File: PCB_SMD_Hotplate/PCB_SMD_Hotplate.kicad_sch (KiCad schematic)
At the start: 17 parts, among them J1 USB_C_Receptacle_USB2.0_16P, J2 CONN_POWER, U1 ATmega328P-A, U2 CH340C, U3 LM7805_TO220, U4 ICL7660, U5 LM324

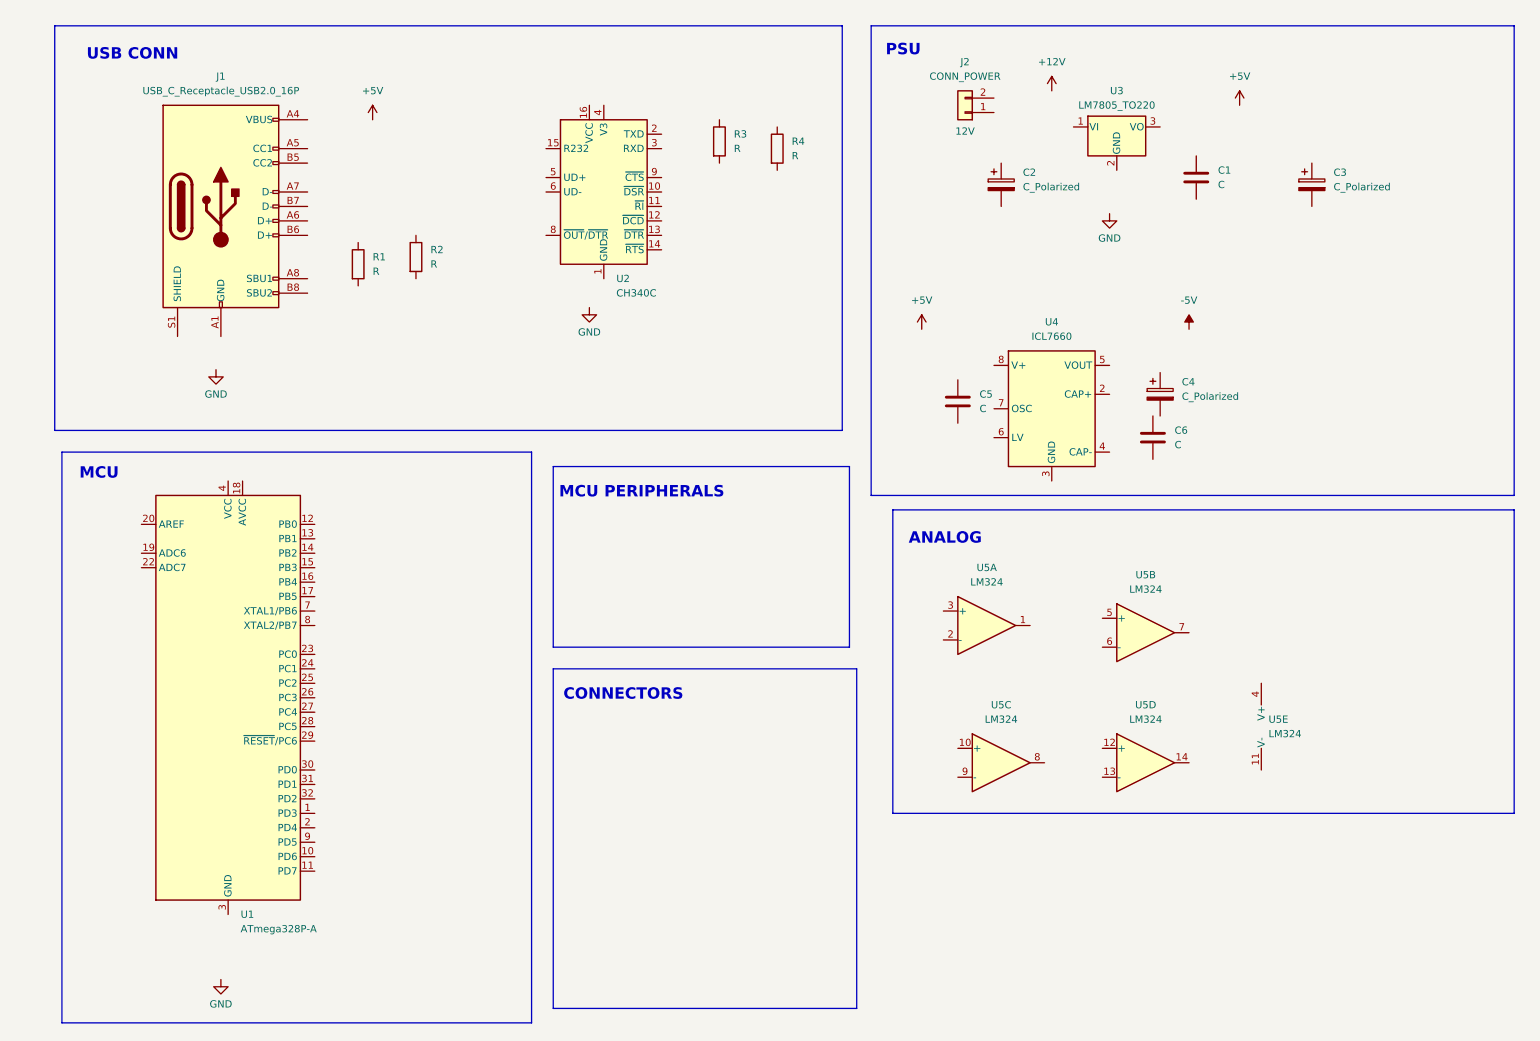
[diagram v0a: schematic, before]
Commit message: Update schematic, start PCB
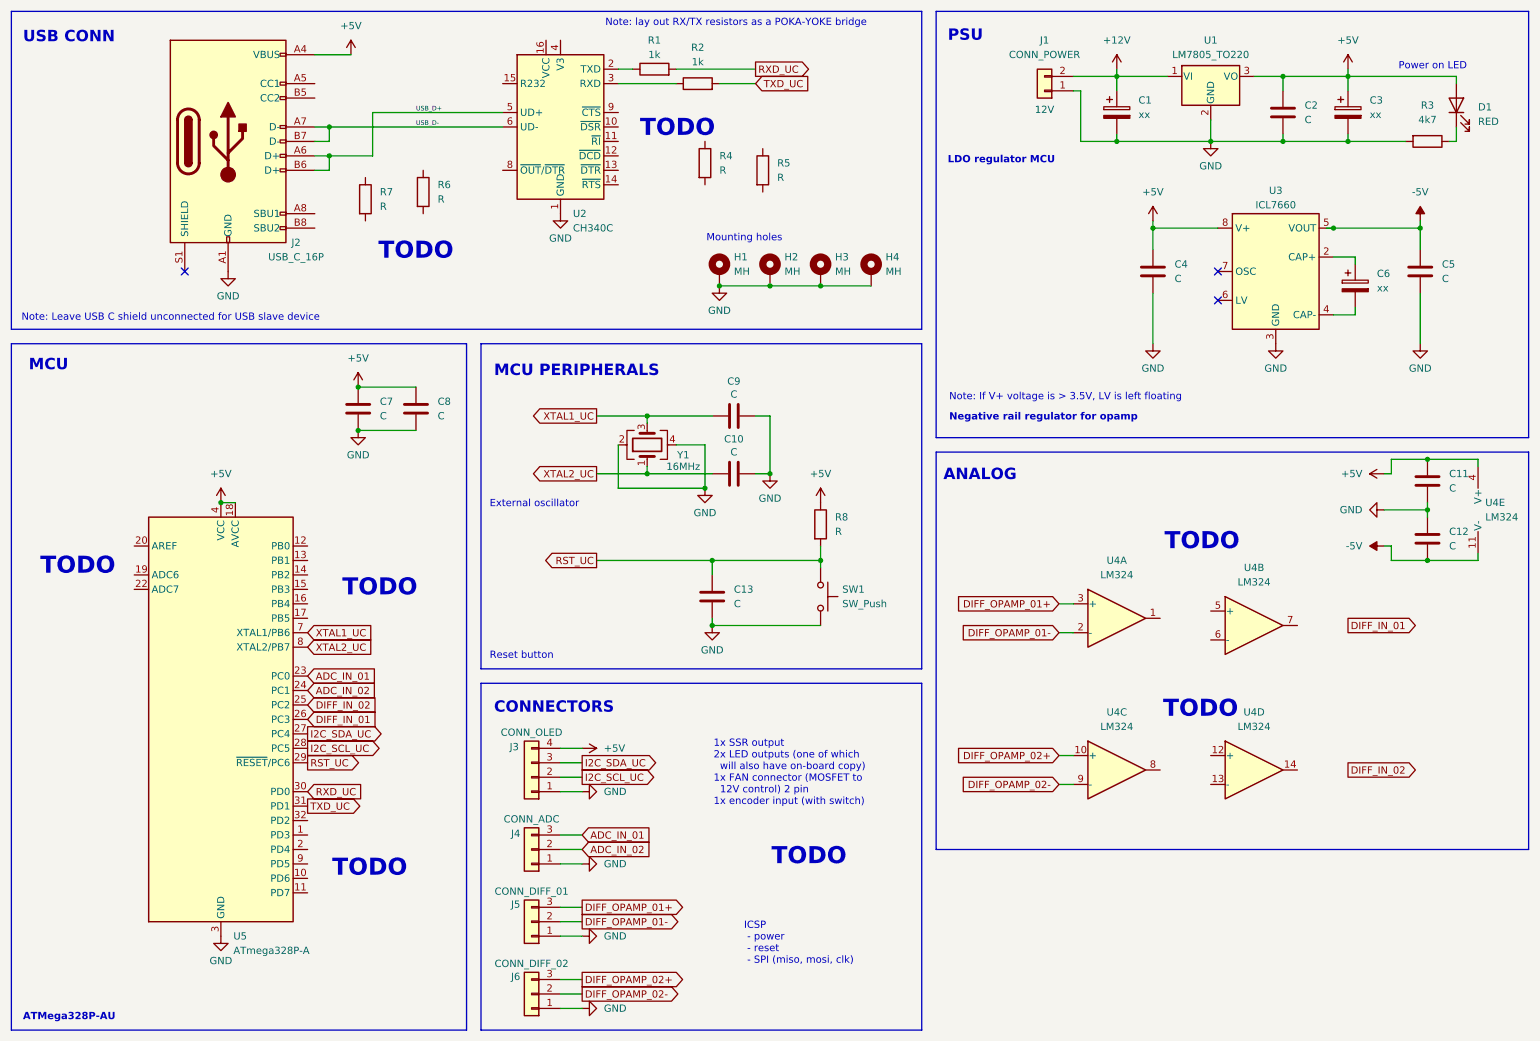
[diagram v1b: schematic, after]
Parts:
- added C10, C11, C12, C13, C7, C8, C9: C, Capacitor_SMD:C_0805_2012Metric, symbol Device:C
- added D1: RED, LED_SMD:LED_1210_3225Metric, symbol Device:LED
- added H1, H2, H3, H4: MH, MountingHole:MountingHole_3.2mm_M3_Pad_Via, symbol Mechanical:MountingHole_Pad
- added J3: CONN_OLED, Connector_PinHeader_2.54mm:PinHeader_1x04_P2.54mm_Vertical, symbol Connector_Generic:Conn_01x04
- added J4: CONN_ADC, Connector_PinHeader_2.54mm:PinHeader_1x03_P2.54mm_Vertical, symbol Connector_Generic:Conn_01x03
- added J5: CONN_DIFF_01, Connector_PinHeader_2.54mm:PinHeader_1x03_P2.54mm_Vertical, symbol Connector_Generic:Conn_01x03
- added J6: CONN_DIFF_02, Connector_PinHeader_2.54mm:PinHeader_1x03_P2.54mm_Vertical, symbol Connector_Generic:Conn_01x03
- added R1, R2: 1k, Resistor_SMD:R_0805_2012Metric, symbol Device:R
- added R3: 4k7, Resistor_SMD:R_0805_2012Metric, symbol Device:R
- added R8: R, Resistor_SMD:R_0805_2012Metric, symbol Device:R
- added SW1: SW_Push, Button_Switch_THT:SW_PUSH_6mm_H4.3mm, symbol Switch:SW_Push
- added Y1: 16MHz, Crystal:Crystal_SMD_3225-4Pin_3.2x2.5mm, symbol Device:Crystal_GND24
- C1: renamed from C2; value C_Polarized -> xx; footprint (none) -> Capacitor_SMD:CP_Elec_6.3x7.7
- C3: value C_Polarized -> xx; footprint (none) -> Capacitor_SMD:CP_Elec_6.3x7.7
- C6: renamed from C4; value C_Polarized -> xx; footprint (none) -> Capacitor_SMD:CP_Elec_6.3x7.7
- J1: renamed from J2; footprint (none) -> Connector_PinHeader_2.54mm:PinHeader_1x02_P2.54mm_Vertical
- J2: renamed from J1; value USB_C_Receptacle_USB2.0_16P -> USB_C_16P
- renumbered C1 to C2, C5 to C4, C6 to C5, R3 to R4, R4 to R5, R2 to R6, R1 to R7, U3 to U1, U4 to U3, U5 to U4, U1 to U5
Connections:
- net +12V: now also C1.1, J1.2 (Pin_2), U1.1 (VI)
- net +5V: now also C2.1, C3.1, C4.1, J2.A4 (VBUS), J2.A9 (VBUS), J2.B4 (VBUS), J2.B9 (VBUS), U1.3 (VO), U3.8 (V+), U4.4 (V+), U5.18 (AVCC), U5.4 (VCC), U5.6 (VCC), C11.1, C7.1, C8.1, D1.2 (A), J3.4 (Pin_4), R8.1
- net -5V: now also C5.1, U3.5 (VOUT), U4.11 (V-), C12.2
- net GND: now also C1.2, C2.2, C3.2, C4.2, C5.2, J1.1 (Pin_1), J2.A1 (GND), J2.A12 (GND), J2.B1 (GND), J2.B12 (GND), U1.2 (GND), U2.1 (GND), U3.3 (GND), U5.21 (GND), U5.3 (GND), U5.5 (GND), C10.1, C11.2, C12.1, C13.2, C7.2, C8.2, C9.1, H1.1, H2.1, H3.1, H4.1, J3.1 (Pin_1), J4.1 (Pin_1), J5.1 (Pin_1), J6.1 (Pin_1), R3.2, SW1.2, Y1.2, Y1.4
- net DIFF_OPAMP_01-: now reaches U4.2 (-)
- net DIFF_OPAMP_01-: now also J5.2 (Pin_2)
- net DIFF_OPAMP_01+: now reaches U4.3 (+)
- net DIFF_OPAMP_01+: now also J5.3 (Pin_3)
- net at U2.2 (TXD): now also R1.1
- net at U2.3 (RXD): now also R2.1
- net USB_D+: now reaches U2.5 (UD+)
- net USB_D+: now also J2.A6 (D+), J2.B6 (D+)
- net USB_D-: now reaches U2.6 (UD-)
- net USB_D-: now also J2.A7 (D-), J2.B7 (D-)
- net DIFF_OPAMP_02+: now reaches U4.10 (+)
- net DIFF_OPAMP_02+: now also J6.3 (Pin_3)
- net DIFF_OPAMP_02-: now reaches U4.9 (-)
- net DIFF_OPAMP_02-: now also J6.2 (Pin_2)
- net ADC_IN_01: now reaches U5.23 (PC0)
- net ADC_IN_01: now also J4.3 (Pin_3)
- net ADC_IN_02: now reaches U5.24 (PC1)
- net ADC_IN_02: now also J4.2 (Pin_2)
- net DIFF_IN_02: now reaches U5.25 (PC2)
- net DIFF_IN_01: now reaches U5.26 (PC3)
- net I2C_SDA_UC: now reaches U5.27 (PC4)
- net I2C_SDA_UC: now also J3.3 (Pin_3)
- net I2C_SCL_UC: now reaches U5.28 (PC5)
- net I2C_SCL_UC: now also J3.2 (Pin_2)
- net RST_UC: now reaches U5.29 (~{RESET}/PC6)
- net RST_UC: now also C13.1, R8.2, SW1.1
- net RXD_UC: now reaches U5.30 (PD0)
- net RXD_UC: now also R1.2
- net TXD_UC: now reaches U5.31 (PD1)
- net TXD_UC: now also R2.2
- net XTAL1_UC: now reaches U5.7 (XTAL1/PB6)
- net XTAL1_UC: now also C9.2, Y1.3
- net XTAL2_UC: now reaches U5.8 (XTAL2/PB7)
- net XTAL2_UC: now also C10.2, Y1.1
- net at C6.1: now also U3.2 (CAP+)
- net at C6.2: now also U3.4 (CAP-)
- new net: D1.1 (K), R3.1
- no-connect marks 0 -> 3
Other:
- note added: "1x SSR output 2x LED outputs (one of which will also have on-board copy) 1x FAN connector (MOSFET to 12V control) 2 pin 1x encoder input (with switch)"
- note added: "ATMega328P-AU"
- note added: "External oscillator"
- note added: "ICSP - power - reset - SPI (miso, mosi, clk)"
- note added: "LDO regulator MCU"
- note added: "Mounting holes"
- note added: "Negative rail regulator for opamp"
- note added: "Note: If V+ voltage is > 3.5V, LV is left floating"
- note added: "Note: Leave USB C shield unconnected for USB slave device"
- note added: "Note: lay out RX/TX resistors as a POKA-YOKE bridge"
- note added: "Power on LED"
- note added: "Reset button"
- note added: "TODO"
- moved on the sheet: C1, C2, C3, C4, C5, C6, J1, J2, R4, R5, R6, R7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

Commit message: Finish schm, finish component layout
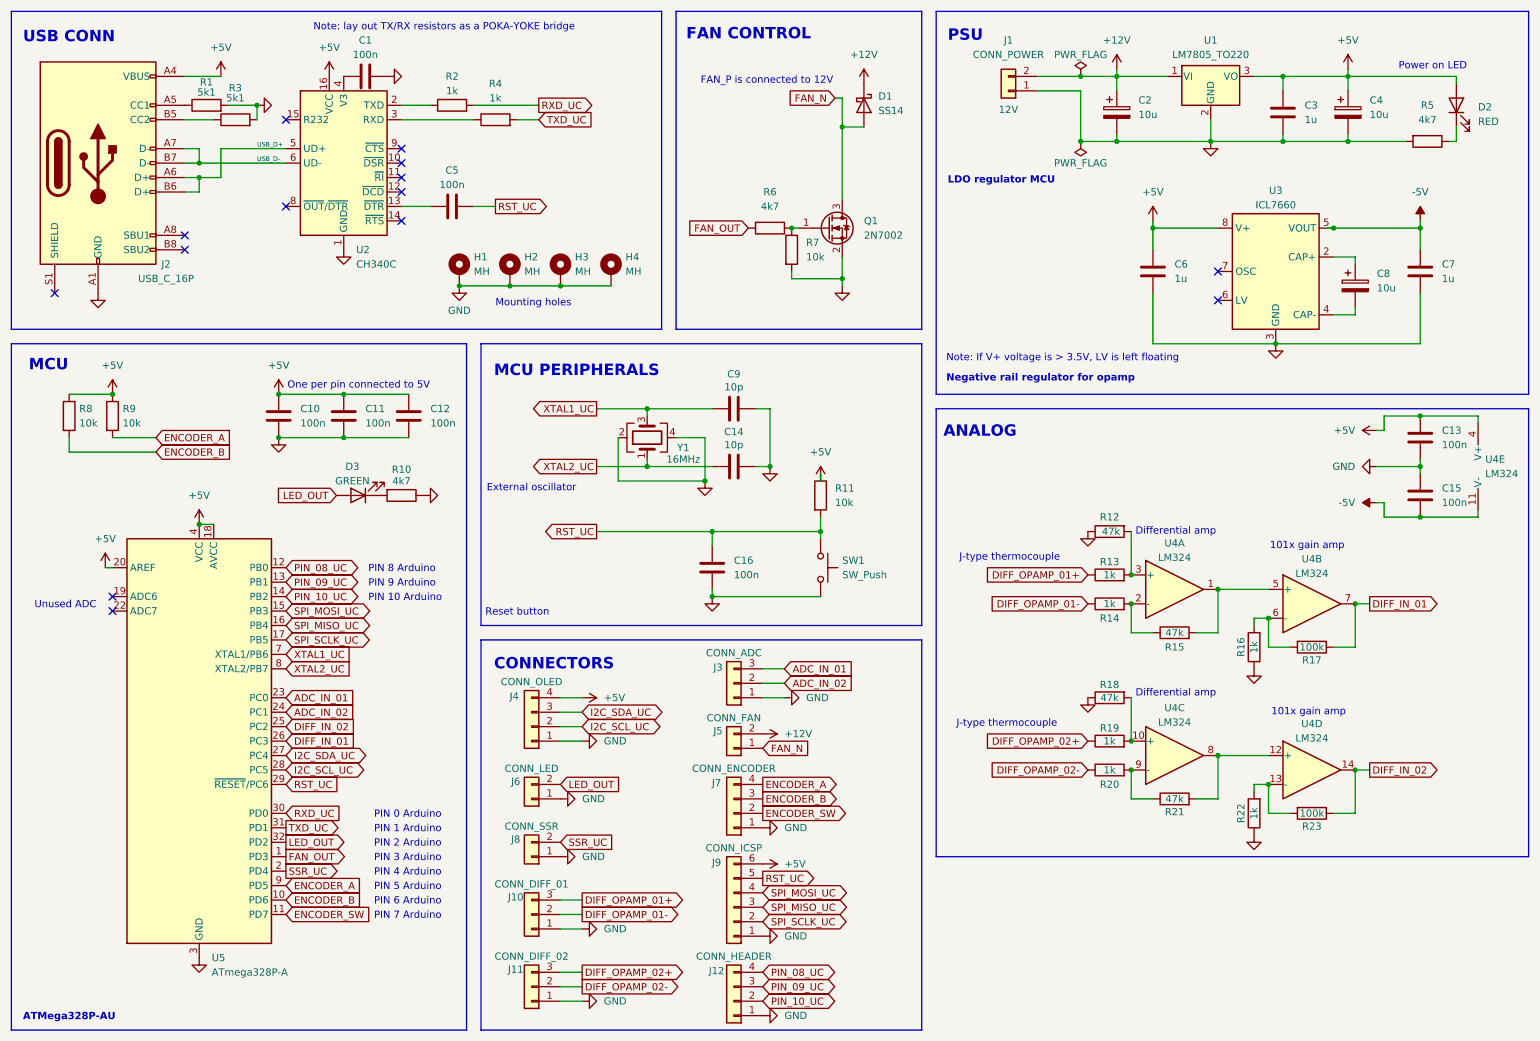
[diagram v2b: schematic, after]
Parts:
- removed R4, R5: R, Resistor_SMD:R_0805_2012Metric, symbol Device:R
- added C1, C12, C5: 100n, Capacitor_SMD:C_0805_2012Metric, symbol Device:C
- added D1: SS14, Diode_SMD:D_SMA, symbol Diode:SS14
- added D3: GREEN, LED_SMD:LED_1210_3225Metric, symbol Device:LED
- added J12: CONN_HEADER, Connector_PinHeader_2.54mm:PinHeader_1x04_P2.54mm_Vertical, symbol Connector_Generic:Conn_01x04
- added J5: CONN_FAN, Connector_PinHeader_2.54mm:PinHeader_1x02_P2.54mm_Vertical, symbol Connector_Generic:Conn_01x02
- added J6: CONN_LED, Connector_PinHeader_2.54mm:PinHeader_1x02_P2.54mm_Vertical, symbol Connector_Generic:Conn_01x02
- added J7: CONN_ENCODER, Connector_PinHeader_2.54mm:PinHeader_1x04_P2.54mm_Vertical, symbol Connector_Generic:Conn_01x04
- added J8: CONN_SSR, Connector_PinHeader_2.54mm:PinHeader_1x02_P2.54mm_Vertical, symbol Connector_Generic:Conn_01x02
- added J9: CONN_ICSP, Connector_PinHeader_2.54mm:PinHeader_1x06_P2.54mm_Vertical, symbol Connector_Generic:Conn_01x06
- added Q1: 2N7002, Package_TO_SOT_SMD:SOT-23, symbol Transistor_FET:2N7002
- added R1, R3: 5k1, Resistor_SMD:R_0805_2012Metric, symbol Device:R
- added R10: 4k7, Resistor_SMD:R_0805_2012Metric, symbol Device:R
- added R12, R15, R18, R21: 47k, Resistor_SMD:R_0805_2012Metric, symbol Device:R
- added R13, R14, R16, R19, R20, R22: 1k, Resistor_SMD:R_0805_2012Metric, symbol Device:R
- added R17, R23: 100k, Resistor_SMD:R_0805_2012Metric, symbol Device:R
- added R8, R9: 10k, Resistor_SMD:R_0805_2012Metric, symbol Device:R
- C10: renamed from C7; value C -> 100n
- C11: renamed from C8; value C -> 100n
- C13: renamed from C11; value C -> 100n
- C14: renamed from C10; value C -> 10p
- C15: renamed from C12; value C -> 100n
- C16: renamed from C13; value C -> 100n
- C2: renamed from C1; value xx -> 10u
- C3: renamed from C2; value C -> 1u
- C4: renamed from C3; value xx -> 10u
- C6: renamed from C4; value C -> 1u
- C7: renamed from C5; value C -> 1u
- C8: renamed from C6; value xx -> 10u
- C9: value C -> 10p
- R11: renamed from R8; value R -> 10k
- R6: value R -> 4k7
- R7: value R -> 10k
- renumbered D1 to D2, J5 to J10, J6 to J11, J4 to J3, J3 to J4, R1 to R2, R2 to R4, R3 to R5
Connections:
- net +12V: now also D1.1 (K), J5.2 (Pin_2)
- net +5V: now also U2.16 (VCC), U5.20 (AREF), C12.1, J9.6 (Pin_6), R8.1, R9.1
- net DIFF_IN_01: now also U4.7, R17.1
- net DIFF_IN_02: now also U4.14, R23.1
- net DIFF_OPAMP_01+: now also R13.1; no longer U4.3 (+)
- net DIFF_OPAMP_01-: now also R14.1; no longer U4.2 (-)
- net DIFF_OPAMP_02+: now also R19.1; no longer U4.10 (+)
- net DIFF_OPAMP_02-: now also R20.1; no longer U4.9 (-)
- net GND: now also R7.2, C1.2, C12.2, J12.1 (Pin_1), J6.1 (Pin_1), J7.1 (Pin_1), J8.1 (Pin_1), J9.1 (Pin_1), Q1.2 (S), R1.2, R10.1, R12.1, R16.1, R18.1, R22.1, R3.2
- net RST_UC: now also C5.2, J9.5 (Pin_5)
- net at R6.1: now also R7.1, Q1.1 (G)
- net FAN_OUT: now reaches R6.2
- net FAN_OUT: now also U5.1 (PD3)
- net at U4.1: now also U4.5 (+), R15.2
- net at U2.13 (~{DTR}): now also C5.1
- net at U2.4 (V3): now also C1.1
- net at J2.A5 (CC1): now also R1.1
- net at J2.B5 (CC2): now also R3.1
- net at U4.8: now also U4.12 (+), R21.2
- net ENCODER_B: now reaches U5.10 (PD6)
- net ENCODER_B: now also J7.3 (Pin_3), R8.2
- net ENCODER_SW: now reaches U5.11 (PD7)
- net ENCODER_SW: now also J7.2 (Pin_2)
- net PIN_08_UC: now reaches U5.12 (PB0)
- net PIN_08_UC: now also J12.4 (Pin_4)
- net PIN_09_UC: now reaches U5.13 (PB1)
- net PIN_09_UC: now also J12.3 (Pin_3)
- net PIN_10_UC: now reaches U5.14 (PB2)
- net PIN_10_UC: now also J12.2 (Pin_2)
- net SPI_MOSI_UC: now reaches U5.15 (PB3)
- net SPI_MOSI_UC: now also J9.4 (Pin_4)
- net SPI_MISO_UC: now reaches U5.16 (PB4)
- net SPI_MISO_UC: now also J9.3 (Pin_3)
- net SPI_SCLK_UC: now reaches U5.17 (PB5)
- net SPI_SCLK_UC: now also J9.2 (Pin_2)
- net SSR_UC: now reaches U5.2 (PD4)
- net SSR_UC: now also J8.2 (Pin_2)
- net LED_OUT: now reaches U5.32 (PD2)
- net LED_OUT: now also D3.2 (A), J6.2 (Pin_2)
- net ENCODER_A: now reaches U5.9 (PD5)
- net ENCODER_A: now also J7.4 (Pin_4), R9.2
- net at U4.6 (-): now also R16.2, R17.2
- net at U4.13 (-): now also R22.2, R23.2
- new net: R14.2, R15.1, U4.2 (-)
- new net: R12.2, R13.2, U4.3 (+)
- new net: R18.2, R19.2, U4.10 (+)
- new net: R20.2, R21.1, U4.9 (-)
- new net: D3.1 (K), R10.2
- new net FAN_N: D1.2 (A), J5.1 (Pin_1), Q1.3 (D)
- no-connect marks 3 -> 14
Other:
- note added: "101x gain amp"
- note added: "Differential amp"
- note added: "FAN CONTROL"
- note added: "FAN_P is connected to 12V"
- note added: "J-type thermocouple"
- note added: "Note: lay out TX/RX resistors as a POKA-YOKE bridge"
- note added: "One per pin connected to 5V"
- note added: "PIN 0 Arduino"
- note added: "PIN 1 Arduino"
- note added: "PIN 10 Arduino"
- note added: "PIN 2 Arduino"
- note added: "PIN 3 Arduino"
- note added: "PIN 4 Arduino"
- note added: "PIN 5 Arduino"
- note added: "PIN 6 Arduino"
- note added: "PIN 7 Arduino"
- note added: "PIN 8 Arduino"
- note added: "PIN 9 Arduino"
- note added: "Unused ADC"
- note removed: "1x SSR output 2x LED outputs (one of which will also have on-board copy) 1x FAN connector (MOSFET to 12V control) 2 pin 1x encoder input (with switch)"
- note removed: "ICSP - power - reset - SPI (miso, mosi, clk)"
- note removed: "Note: Leave USB C shield unconnected for USB slave device"
- note removed: "Note: lay out RX/TX resistors as a POKA-YOKE bridge"
- note removed: "TODO"
- moved on the sheet: C10, C11, C13, C14, C15, C16, C9, H1, H2, H3, H4, J1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

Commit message: Finish layout and routing
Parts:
- removed C12: 100n, Capacitor_SMD:C_0805_2012Metric, symbol Device:C
- renumbered C13 to C12, C14 to C13, C15 to C14, C16 to C15
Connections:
- net ENCODER_A: now also U5.11 (PD7); no longer U5.9 (PD5)
- net ENCODER_SW: now also U5.9 (PD5); no longer U5.11 (PD7)
- net PIN_08_UC: now also J12.2 (Pin_2); no longer J12.4 (Pin_4)
- net PIN_10_UC: now also J12.4 (Pin_4); no longer J12.2 (Pin_2)
- net SPI_MOSI_UC: now also J9.2 (Pin_2); no longer J9.4 (Pin_4)
- net SPI_SCLK_UC: now also J9.4 (Pin_4); no longer J9.2 (Pin_2)
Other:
- note removed: "One per pin connected to 5V"
- moved on the sheet: C10, C11
